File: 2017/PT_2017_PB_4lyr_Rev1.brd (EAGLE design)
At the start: 162.5 x 209.5 mm, 161 parts, among them J1 APP_2POS_CONFIG12V_VERT, J2 APP_2POS_CONFIG12V_VERT, J3 APP_2POS_CONFIG12V_VERT, J4 APP_2POS_CONFIG12V_VERT, Q1 2N7002PW, Q12 2N7002, X1 22-23-2021

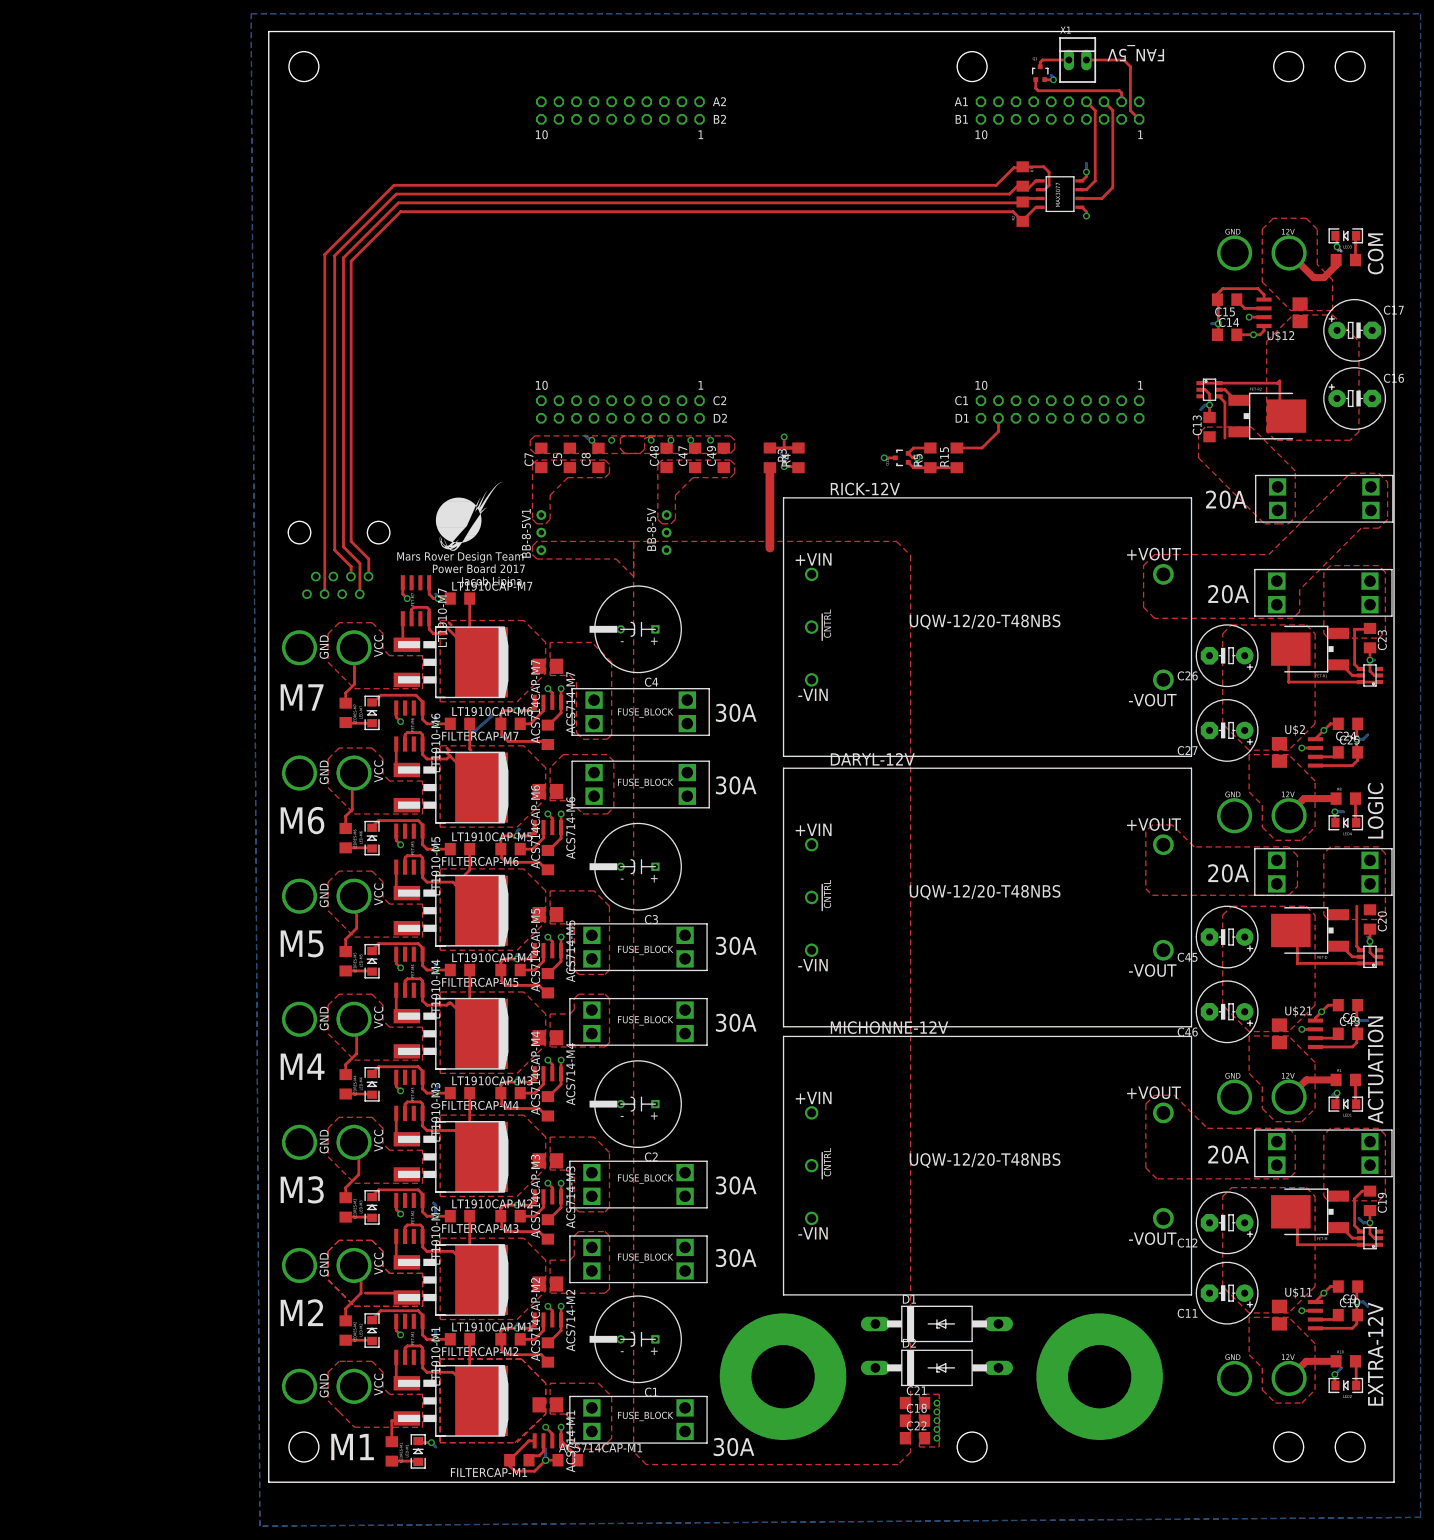
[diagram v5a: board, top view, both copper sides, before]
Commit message: Fixed All Vias
Moved vias away from pads to prevent solder bridging and unrouted
dead-end traces resulting from pulling traces to other layers.
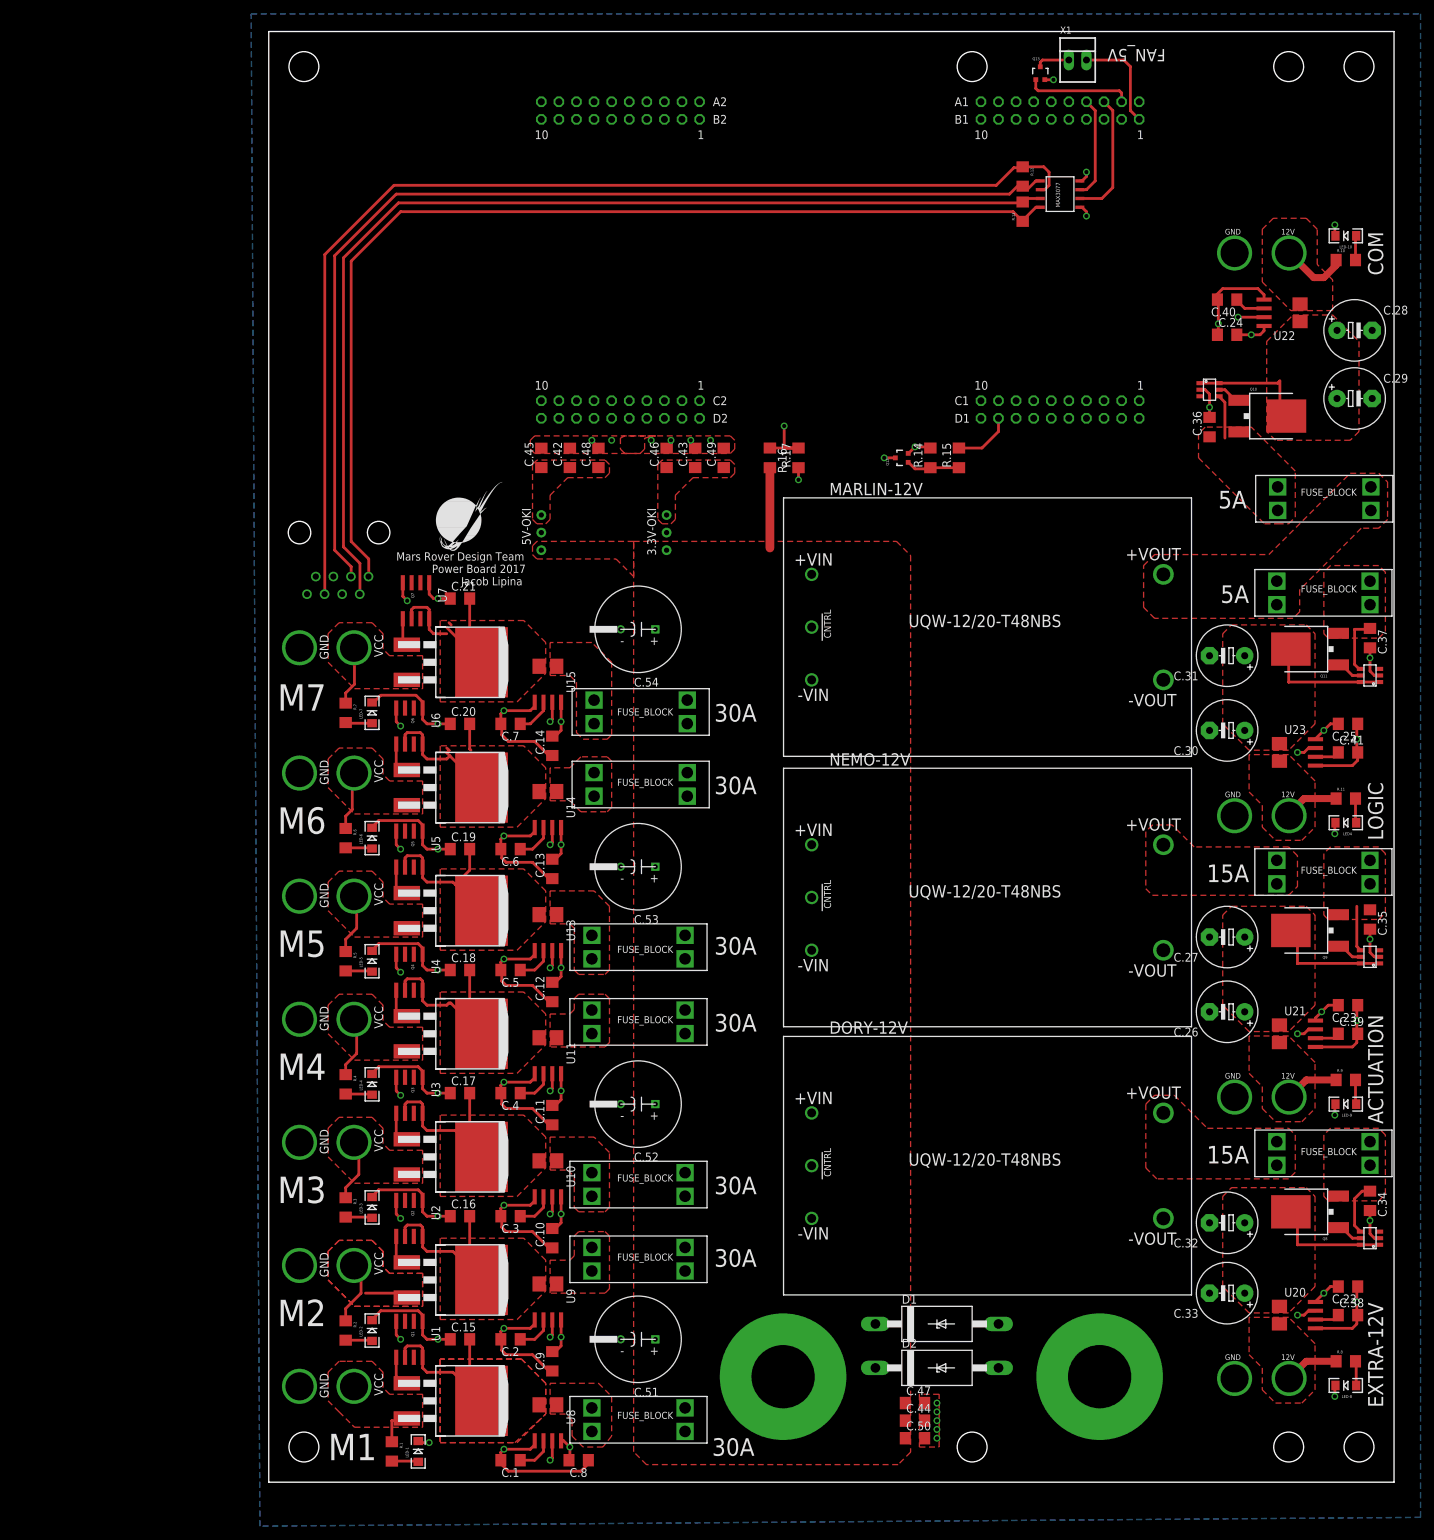
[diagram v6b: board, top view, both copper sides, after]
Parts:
- removed ACS714CAP-M1, ACS714CAP-M2, ACS714CAP-M3, ACS714CAP-M4, ACS714CAP-M5, ACS714CAP-M6, ACS714CAP-M7: .1µF, resistor:C1206
- removed FET-M1: Q_IRFS7437PbF, MRDT-2015-PowerBoard:D2PACK
- removed FILTERCAP-M1: 1nF, resistor:C1206
- removed R15: 1k, resistor:R1206
- added C.1: 1nF, resistor:C1206
- added C.10, C.11, C.12, C.13, C.14, C.8, C.9: .1µF, resistor:C1206
- added Q13: 2N7002PW, SparkFun-DiscreteSemi:SOT323
- added R.15: 1k, resistor:R1206
- Q1: value 2N7002PW -> Q_IRFS7437PbF; device SparkFun-DiscreteSemi:SOT323 -> MRDT-2015-PowerBoard:D2PACK
- moved Q1 206.1 mm to (24.1, 16.8), turned to 270 degrees
- moved U$40 1.27 mm to (157.5, 5.08)
- moved U$8 1.27 mm to (157.5, 204.5)
- renumbered ACS714-M1 to U8, ACS714-M2 to U9, ACS714-M3 to U10, ACS714-M4 to U11, ACS714-M5 to U13, ACS714-M6 to U14, ACS714-M7 to U15, BB-8-5V to 3.3V-OKI, BB-8-5V1 to 5V-OKI, C1 to C.51, C10 to C.38, C11 to C.33, C12 to C.32, C13 to C.36, C14 to C.24, C15 to C.40, C16 to C.29, C17 to C.28, C18 to C.44, C19 to C.34, C2 to C.52, C20 to C.35, C21 to C.47, C22 to C.50, C23 to C.37, C24 to C.25, C25 to C.41, C26 to C.31, C27 to C.30, C3 to C.53, C4 to C.54, C43 to C.39, C45 to C.27, C46 to C.26, C47 to C.43, C48 to C.46, C49 to C.49, C5 to C.42, C6 to C.23, C7 to C.45, C8 to C.48, C9 to C.22, DARYL-12V to NEMO-12V, FET-D to Q9, FET-M to Q8, FET-M2 to Q2, FET-M3 to Q3, FET-M4 to Q4, FET-M5 to Q5, FET-M6 to Q6, FET-M7 to Q7, FET-R1 to Q11, FET-R2 to Q10, FILTERCAP-M2 to C.2, FILTERCAP-M3 to C.3, FILTERCAP-M4 to C.4, FILTERCAP-M5 to C.5, FILTERCAP-M6 to C.6, FILTERCAP-M7 to C.7, LED-M1 to LED-1, LED-M2 to LED-2, LED-M3 to LED-3, LED-M4 to LED-4, LED-M5 to LED-5, LED-M6 to LED-6, LED-M7 to LED-7, LED1 to LED-9, LED2 to LED-8, LED3 to LED-10, LEDRES-M1 to R.1, LEDRES-M2 to R.2, LEDRES-M3 to R.3, LEDRES-M4 to R.4, LEDRES-M5 to R.5, LEDRES-M6 to R.6, LEDRES-M7 to R.7, LT1910-M1 to U1, LT1910-M2 to U2, LT1910-M3 to U3, LT1910-M4 to U4, LT1910-M5 to U5, LT1910-M6 to U6, LT1910-M7 to U7, LT1910CAP-M1 to C.15, LT1910CAP-M2 to C.16, LT1910CAP-M3 to C.17, LT1910CAP-M4 to C.18, LT1910CAP-M5 to C.19, LT1910CAP-M6 to C.20, LT1910CAP-M7 to C.21, MICHONNE-12V to DORY-12V, R1 to R.9, R10 to R.8, R2 to R.13, R3 to R.16, R4 to R.17, R5 to R.14, R6 to R.10, R7 to R.12, R8 to R.11, RICK-12V to MARLIN-12V, U$11 to U20, U$12 to U22, U$13 to U18, U$2 to U23, U$21 to U21, U$24 to U24, U$4 to U19, U$42 to RJ45, U$6 to U17, U$9 to U16
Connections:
- net 3.3V: now also C.10.2, C.11.2, C.12.2, C.13.2, C.14.2, C.8.2, C.9.2; no longer ACS714CAP-M1.2, ACS714CAP-M2.2, ACS714CAP-M3.2, ACS714CAP-M4.2, ACS714CAP-M5.2, ACS714CAP-M6.2, ACS714CAP-M7.2
- net DRAIN-M1: now also Q1.TAB; no longer FET-M1.TAB
- net FAN_CTL_1: now also Q13.1; no longer Q1.1
- net FILTER-M1: now also C.1.1; no longer FILTERCAP-M1.1
- net GATE-M1: now also Q1.1; no longer FET-M1.1
- net GND: now also C.1.2, C.10.1, C.11.1, C.12.1, C.13.1, C.14.1, C.8.1, C.9.1, Q13.2; no longer ACS714CAP-M1.1, ACS714CAP-M2.1, ACS714CAP-M3.1, ACS714CAP-M4.1, ACS714CAP-M5.1, ACS714CAP-M6.1, ACS714CAP-M7.1, FILTERCAP-M1.2, Q1.2
- net N$114: now also R.15.1; no longer R15.1
- net N$66: now also Q13.3; no longer Q1.3
- net SIG-12V: now also R.15.2; no longer R15.2
- net SOURCE-M1: now also Q1.2; no longer FET-M1.2
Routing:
- net 3.3V: track 123.9 -> 55.8 mm
- net GND: track 336.2 -> 310.8 mm
- net IMEAS-M7: track 110.2 -> 113.8 mm
- net IMEAS-M1: track 212.8 -> 216.4 mm
- net IMEAS-M5: track 144.5 -> 147.6 mm
- net IMEAS-M4: track 165.0 -> 168.1 mm
- net IMEAS-M6: track 127.5 -> 130.6 mm
- net IMEAS-M3: track 179.4 -> 182.5 mm
- net IMEAS-M2: track 196.4 -> 199.5 mm
- net SIG-M1: track 157.5 -> 158.8 mm
- net SIG-M6: track 62.7 -> 64.0 mm
- net SIG-M5: track 81.9 -> 83.2 mm
- net SIG-M4: track 97.1 -> 98.4 mm
- net SIG-M3: track 118.5 -> 119.8 mm
- net SIG-M2: track 133.4 -> 134.7 mm
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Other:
- board text added: "15A"
- board text added: "5A"
- board text removed: "20A"

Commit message: Placed Component Names on Board
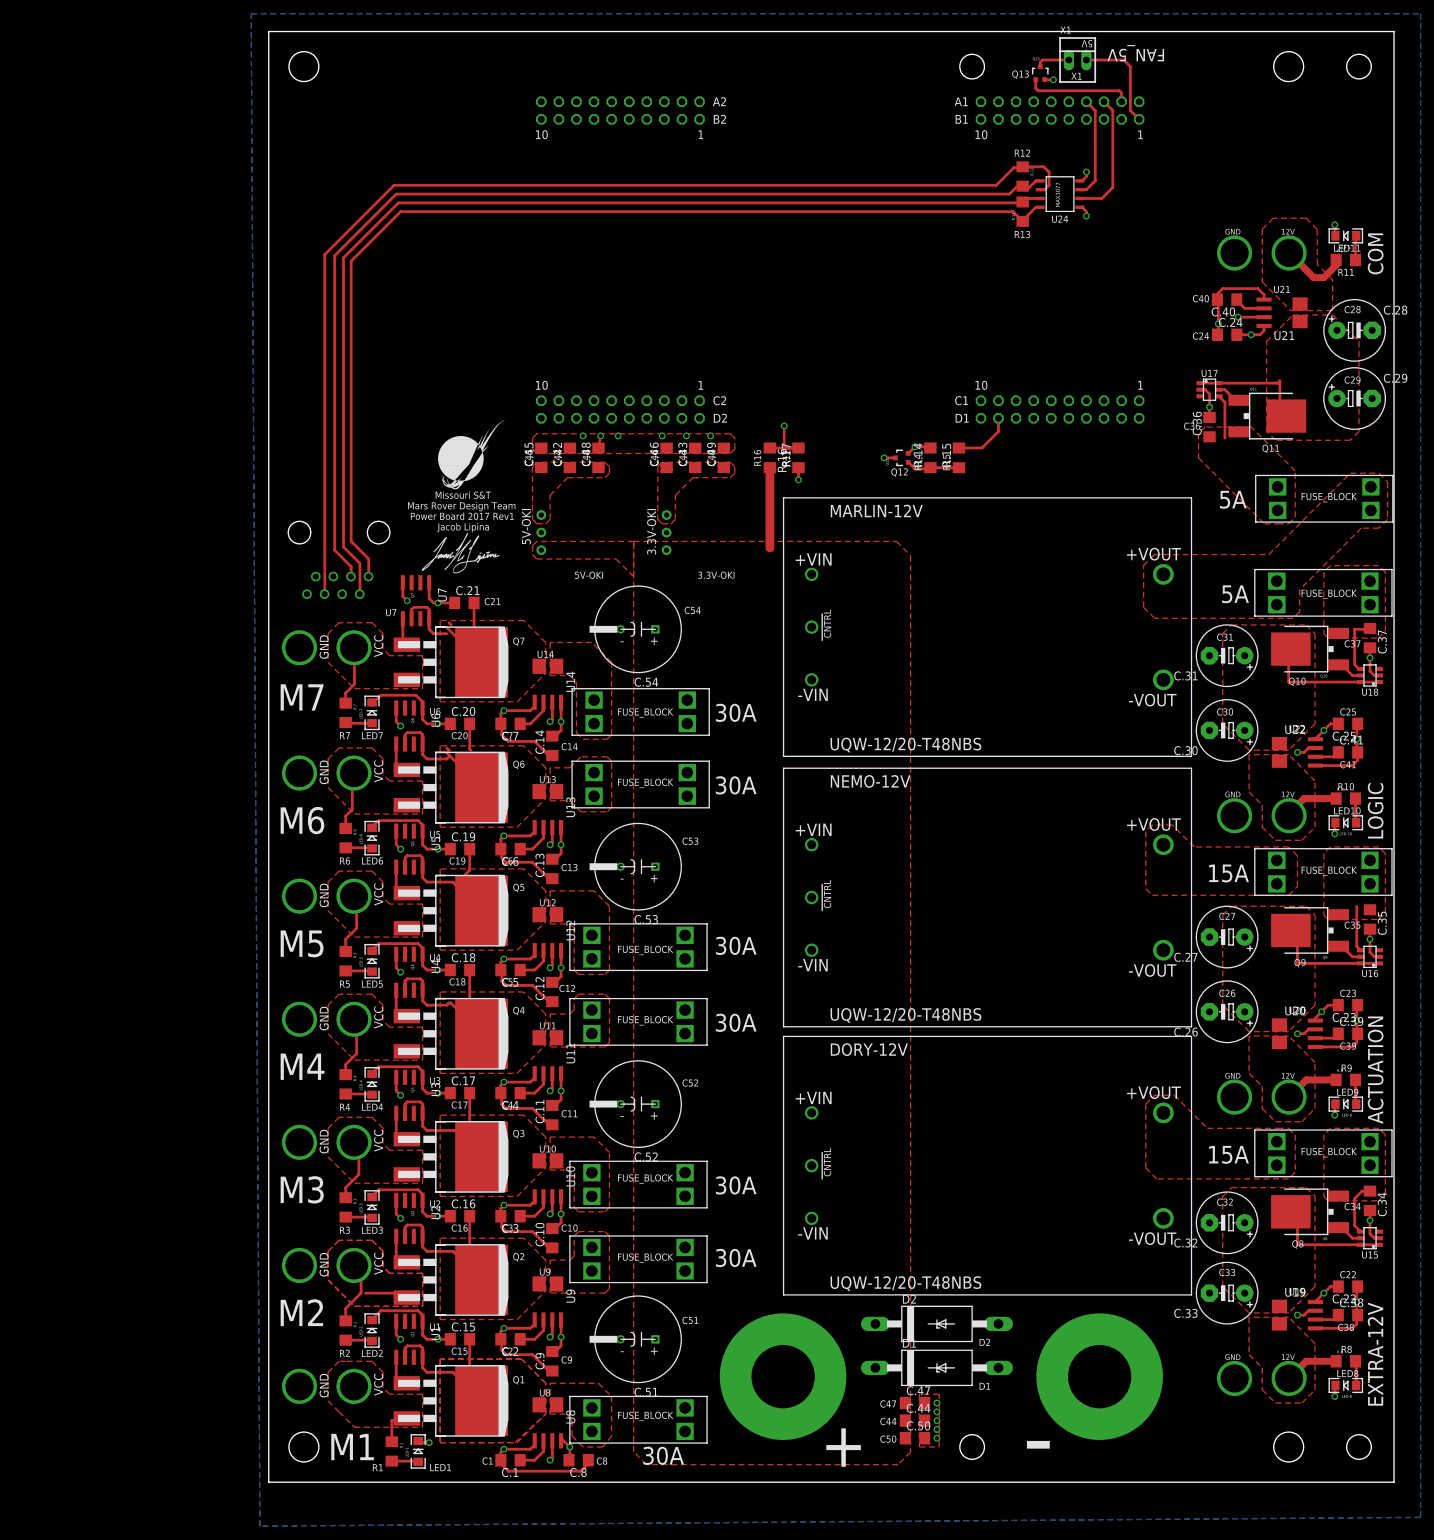
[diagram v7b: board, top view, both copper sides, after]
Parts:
- removed LED4: (no value), SparkFun-LED:LED-1206
- removed U23: ACS714LLCTR-50A-T, MRDT-2015-PowerBoard:SOIC8_ACS711
- added LED-11: (no value), SparkFun-LED:LED-1206
- added U$2: JACOB_SIG, Jacob Signature:JACOB_SIG
- added U12: ACS722LLCTR-40AU-T, MRDT-2015-PowerBoard:SOIC8_ACS711
- U$34, U$35, U$40, U$8: value MOUNTING_HOLE#8 -> MOUNTING_HOLE#6; device MRDT-Hardware:#8_SCREW -> MRDT-Hardware:#6_SCREW
- U10, U11, U13, U14, U20, U21, U22, U8, U9: value ACS714LLCTR-50A-T -> ACS722LLCTR-40AU-T
- U15: value ACS714LLCTR-50A-T -> LM5050; device MRDT-2015-PowerBoard:SOIC8_ACS711 -> LM5050:LM5050
- U19: value LM5050 -> ACS722LLCTR-40AU-T; device LM5050:LM5050 -> MRDT-2015-PowerBoard:SOIC8_ACS711
- moved U15 143.2 mm to (159.1, 35.2), turned to 90 degrees
- moved U21 104.2 mm to (146.4, 168.9), turned to 90 degrees
- moved U19 93.0 mm to (148.6, 24.1), turned to 270 degrees
- moved U17 85.1 mm to (135.9, 157.8), turned to 270 degrees
- moved LED-10 84.8 mm to (155.6, 95.2)
- moved R.10 77.8 mm to (155.6, 98.7)
- moved R.11 77.8 mm to (155.6, 176.5)
- moved U22 63.5 mm to (148.6, 105.4), turned to 270 degrees
- moved U18 47.3 mm to (159.1, 116.5), turned to 90 degrees
- moved U20 40.6 mm to (148.6, 64.8)
- moved U16 40.6 mm to (159.1, 75.9)
- moved Q10 33.9 mm to (149.2, 120.3), turned to 90 degrees
- moved Q11 33.9 mm to (145.4, 154.0), turned to 270 degrees
- moved U14 18.1 mm to (40.3, 115.3)
- moved U13 17.8 mm to (40.3, 97.2)
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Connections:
- removed net IMEAS-M8: U$1.PD2
- removed net N$16 (its old number): LED4.A, R.11.2
- removed net N$20 (its old number): Q11.1, U19.P$2
- removed net N$98: U$1.+3V3_1, U$1.+3V3_2
- removed net RX2: U$1.PP0
- removed net TX2: U$1.PP1
- new net N$17: Q11.1, U17.P$2
- new net N$7: LED-11.A, R.11.2
- net 12V-AUX-ACT: now also U20.4; no longer U21.4
- net 12V-AUX-COM: now also R.10.1, U22.4; no longer R.11.1, U23.4
- net 12V-AUX-EXTRA: now also U19.4; no longer U20.4
- net 12V-AUX-LOGIC: now also R.11.1, U21.4; no longer R.10.1, U22.4
- net 3.3V: now also U$1.+3V3_1, U$1.+3V3_2, U12.8, U19.8; no longer U15.8, U23.8
- net ACT-12V-SIG: now also U20.7; no longer U21.7
- net COM-12V-SIG: now also U22.7; no longer U23.7
- net DRAIN-M5: now also U12.4; no longer U13.4
- net DRAIN-M6: now also U13.4; no longer U14.4
- net DRAIN-M7: now also U14.4; no longer U15.4
- net EXTRA-12V-SIG: now also U19.7; no longer U20.7
- net FILTER-M5: now also U12.6; no longer U13.6
- net FILTER-M6: now also U13.6; no longer U14.6
- net FILTER-M7: now also U14.6; no longer U15.6
- net GND: now also LED-11.C, U12.5, U15.P$1, U19.5; no longer LED4.C, U15.5, U19.P$1, U23.5
- net IMEAS-M5: now also U12.7; no longer U13.7
- net IMEAS-M6: now also U13.7; no longer U14.7
- net IMEAS-M7: now also U14.7; no longer U15.7
- net LOGIC-12V-SIG: now also U21.7; no longer U22.7
- net N$1: now also U16.P$6; no longer U17.P$6
- net N$10: now also U19.6; no longer U20.6
- net N$11: now also U15.P$4, U15.P$5, U19.1; no longer U16.P$4, U16.P$5, U20.1
- net N$12: now also U20.6; no longer U21.6
- net N$13: now also Q11.3, U17.P$6; no longer Q10.3, U18.P$6
- net N$14: now also U16.P$4, U16.P$5, U20.1; no longer U17.P$4, U17.P$5, U21.1
- net N$15: now also U21.6; no longer U22.6
- net N$19: now also Q11.4, U17.P$4, U17.P$5, U21.1; no longer Q10.4, U18.P$4, U18.P$5, U22.1
- net N$2: now also U15.P$6; no longer U16.P$6
- net N$22: now also Q10.4, U18.P$4, U18.P$5, U22.1; no longer Q11.4, U19.P$4, U19.P$5, U23.1
- net N$3: now also U16.P$2; no longer U17.P$2
- net N$4: now also U22.6; no longer U23.6
- net N$5: now also U15.P$2; no longer U16.P$2
- net N$9: now also Q10.3, U18.P$6; no longer Q11.3, U19.P$6
- net SIG-M1: now also U$1.PP5; no longer U$1.PA7
- net SIG-M2: now also U$1.PA7; no longer U$1.PH0
- net SIG-M3: now also U$1.PH0; no longer U$1.PP3
- net SIG-M4: now also U$1.PP3; no longer U$1.PQ1
- net V_BATT_M5: now also U12.1; no longer U13.1
- net V_BATT_M6: now also U13.1; no longer U14.1
- net V_BATT_M7: now also U14.1; no longer U15.1
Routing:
- net SIG-M2: track 134.7 -> 141.9 mm
- net N$20 (its old number): track 3.86 -> 0.00 mm
- net N$7: track 0.00 -> 3.53 mm
- net N$16 (its old number): track 3.53 -> 0.00 mm
- net N$17: track 0.00 -> 3.50 mm
- net SIG-M1: track 158.8 -> 161.3 mm
- net GND: track 310.8 -> 312.4 mm
- net DRAIN-M7: track 21.9 -> 22.8 mm
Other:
- board text added: "+"
- board text added: "-"
- board text added: "3.3V-OKI"
- board text added: "5V"
- board text added: "5V-OKI"
- board text added: "C1"
- board text added: "C10"
- board text added: "C11"
- board text added: "C12"
- board text added: "C13"
- board text added: "C14"
- board text added: "C15"
- board text added: "C16"
- board text added: "C17"
- board text added: "C18"
- board text added: "C19"
- board text added: "C2"
- board text added: "C20"
- board text added: "C21"
- board text added: "C22"
- board text added: "C23"
- board text added: "C24"
- board text added: "C25"
- board text added: "C26"
- board text added: "C27"
- board text added: "C28"
- board text added: "C29"
- board text added: "C3"
- board text added: "C30"
- board text added: "C31"
- board text added: "C32"
- board text added: "C33"
- board text added: "C34"
- board text added: "C35"
- board text added: "C36"
- board text added: "C37"
- board text added: "C38"
- board text added: "C39"
- board text added: "C4"
- board text added: "C40"
- board text added: "C41"
- board text added: "C42"
- board text added: "C43"
- board text added: "C44"
- board text added: "C45"
- board text added: "C46"
- board text added: "C47"
- board text added: "C48"
- board text added: "C49"
- board text added: "C5"
- board text added: "C50"
- board text added: "C51"
- board text added: "C52"
- board text added: "C53"
- board text added: "C54"
- board text added: "C6"
- board text added: "C7"
- board text added: "C8"
- board text added: "C9"
- board text added: "D1"
- board text added: "D2"
- board text added: "LED1"
- board text added: "LED10"
- board text added: "LED11"
- board text added: "LED2"
- board text added: "LED3"
- board text added: "LED4"
- board text added: "LED5"
- board text added: "LED6"
- board text added: "LED7"
- board text added: "LED8"
- board text added: "LED9"
- board text added: "Missouri S&T Mars Rover Design Team Power Board 2017 Rev1 Jacob Lipina"
- board text added: "Q1"
- board text added: "Q10"
- board text added: "Q11"
- board text added: "Q12"
- board text added: "Q13"
- board text added: "Q2"
- board text added: "Q3"
- board text added: "Q4"
- board text added: "Q5"
- board text added: "Q6"
- board text added: "Q7"
- board text added: "Q8"
- board text added: "Q9"
- board text added: "R1"
- board text added: "R10"
- board text added: "R11"
- board text added: "R12"
- board text added: "R13"
- board text added: "R14"
- board text added: "R15"
- board text added: "R16"
- board text added: "R17"
- board text added: "R2"
- board text added: "R3"
- board text added: "R4"
- board text added: "R5"
- board text added: "R6"
- board text added: "R7"
- board text added: "R8"
- board text added: "R9"
- board text added: "U1"
- board text added: "U10"
- board text added: "U11"
- board text added: "U12"
- board text added: "U13"
- board text added: "U14"
- board text added: "U15"
- board text added: "U16"
- board text added: "U17"
- board text added: "U18"
- board text added: "U19"
- board text added: "U2"
- board text added: "U20"
- board text added: "U21"
- board text added: "U22"
- board text added: "U24"
- board text added: "U3"
- board text added: "U4"
- board text added: "U5"
- board text added: "U6"
- board text added: "U7"
- board text added: "U8"
- board text added: "U9"
- board text added: "X1"
- board text removed: "Mars Rover Design Team Power Board 2017 Jacob Lipina"
